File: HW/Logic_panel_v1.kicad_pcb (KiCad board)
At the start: 4 copper layers, 100.1 x 100 mm, 251 parts, among them J1 USB_B_Micro, Q1 Q_NPN_BEC, Q2 Q_NPN_BEC, Q4 Q_NMOS_GSD, Q5 Q_PMOS_GSD, Q6 Q_NMOS_GSD, Q7 Q_PMOS_GSD, Q8 Q_NMOS_GSD, Q9 Q_PMOS_GSD, SW1 SW_SPDT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

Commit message: nicer routing
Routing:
- net Board_1-DATA_hodnoceni_LED: track 88.8 -> 83.7 mm
- net Board_1-BTN_ENTER: track 119.6 -> 115.3 mm
- net Board_1-BARVA_3: track 61.2 -> 56.9 mm
- net Board_1-BARVA_1: track 55.8 -> 51.6 mm
- net Board_1-BARVA_2: track 53.6 -> 49.4 mm
- net Board_1-BTN_NEW_GAME: track 97.0 -> 93.2 mm
- net Board_1-BARVA_5: track 92.9 -> 89.3 mm
- net Board_1-BARVA_4: track 88.8 -> 85.4 mm
- net Board_1-ZAPINANI_2_CAST_LED: track 46.6 -> 44.6 mm
- net Board_1-BARVA_6: track 82.6 -> 80.9 mm
- net Board_1-BTN_SIPKA_VPRAVO: track 42.7 -> 41.4 mm
- net Board_1-EN: track 21.5 -> 20.7 mm

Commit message: repair mistakes
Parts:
- C22: value 4u7 -> 10u
- R15, R17, R19: value 10k -> 100k
- R6: value 2k -> 10k
- R8, R9: value 47k -> 10k
- moved C5 10.8 mm to (64.4, 111.1), turned to 180 degrees
- moved C6 9.47 mm to (53.9, 108.1), turned to 90 degrees
- moved D1 7.06 mm to (67.7, 61.0), turned to 90 degrees
- moved R2 6.98 mm to (67.7, 63.6), turned to 90 degrees
- moved C3 5.16 mm to (64.3, 107.0)
- moved C2 4.53 mm to (63.8, 105.3), turned to 90 degrees
- moved SW1 3.85 mm to (64.2, 52.7)
- moved J1 3.41 mm to (54.3, 67.8)
- moved D7 2.01 mm to (62.1, 65.6)
- moved D8 2.00 mm to (62.1, 63.6)
- moved R18 1.24 mm to (69.9, 108.9)
- moved R17 0.68 mm to (70.1, 91.5)
- moved R19 0.67 mm to (70.0, 113.4)
- moved R8 0.56 mm to (55.0, 92.3)
- moved C4 0.53 mm to (59.8, 102.8)
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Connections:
- J1 pad 6: Board_1-GND -> Board_1-Net-(J1-Pad6)
- R8 pad 2: Board_1-TX_ESP -> Board_1-Net-(R8-Pad2)
- R9 pad 2: Board_1-RX_ESP -> Board_1-Net-(R9-Pad2)
- U2 pad 18: Board_1-Net-(U2-Pad18) -> Board_1-Net-(R9-Pad2)
- U2 pad 19: Board_1-Net-(U2-Pad19) -> Board_1-Net-(R8-Pad2)
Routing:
- net Board_1-+5V: track 86.9 -> 29.2 mm, vias 4 -> 5
- net Board_1-Net-(R9-Pad2): track 0.00 -> 18.4 mm, vias 0 -> 2
- net Board_1-Net-(J1-Pad6): track 0.00 -> 15.5 mm
- net Board_1-Net-(R8-Pad2): track 0.00 -> 13.2 mm, vias 0 -> 2
- net Board_1-DATA_hodnoceni_LED: track 83.7 -> 91.7 mm, vias 2 -> 0
- net Board_1-V_IN: track 13.8 -> 21.3 mm, vias 1 -> 0
- net Board_1-Net-(D8-Pad2): track 23.8 -> 30.2 mm, vias 2 -> 4
- net Board_1-RX_ESP: track 32.1 -> 35.7 mm
- net Board_1-TX_ESP: track 35.1 -> 38.5 mm
- net Board_1-BTN_END: track 23.9 -> 26.1 mm
- net Board_1-BARVA_1: track 51.6 -> 53.6 mm
- net Board_1-BTN_NEW_GAME: track 93.2 -> 94.7 mm
- net Board_1-BTN_ENTER: track 115.3 -> 116.8 mm
- net Board_1-+3V3: track 55.1 -> 56.4 mm, vias 12 -> 11
- net Board_1-GND: track 519.2 -> 518.0 mm, vias 119 -> 123
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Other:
- board text added: "Fialová"
- board text added: "Konec"
- board text added: "Modrá"
- board text added: "Nová hra"
- board text added: "Oranžová"
- board text added: "Potvrdit tah"
- board text added: "Zelená"
- board text added: "Červená"
- board text added: "Šipka vlevo"
- board text added: "Šipka vpravo"
- board text added: "Žlutá"

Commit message: v1.0 for fab
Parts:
- removed the REF** at (58.0, 148.0)
- removed the REF** at (142.1, 52.0)
- added REF**: NPTH, NPTH, F.Cu at (58.0, 148.0)
- added REF**: NPTH, NPTH, F.Cu at (142.0, 52.0)
- moved D8 2.11 mm to (62.0, 65.7)
- moved D7 1.95 mm to (62.0, 63.6)
- moved R16 1.35 mm to (70.1, 87.9)
- moved C22 0.36 mm to (61.7, 81.4)
- moved C23 0.28 mm to (60.6, 81.4)
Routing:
- net Board_1-+3V3: track 56.4 -> 69.1 mm
- net Board_1-Net-(D8-Pad2): track 30.2 -> 24.7 mm, vias 4 -> 2
- net Board_1-Net-(D7-Pad2): track 23.9 -> 28.6 mm
- net Board_1-GND: track 518.0 -> 514.4 mm, vias 123 -> 122
- net Board_1-V_IN: track 21.3 -> 19.5 mm
- net Board_1-/herni_LED.sch/8.sch/DATA_IN: track 40.2 -> 38.8 mm
- net Board_1-V_LED_3: track 206.6 -> 207.4 mm
- net Board_1-V_LED_1: track 302.1 -> 301.3 mm
- net Board_1-ZAPINANI_2_CAST_LED: track 43.8 -> 43.2 mm
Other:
- board size 100.1 x 100 mm -> 100 x 100 mm
- board text added: "Power 3V3"
- board text added: "Power 5V"

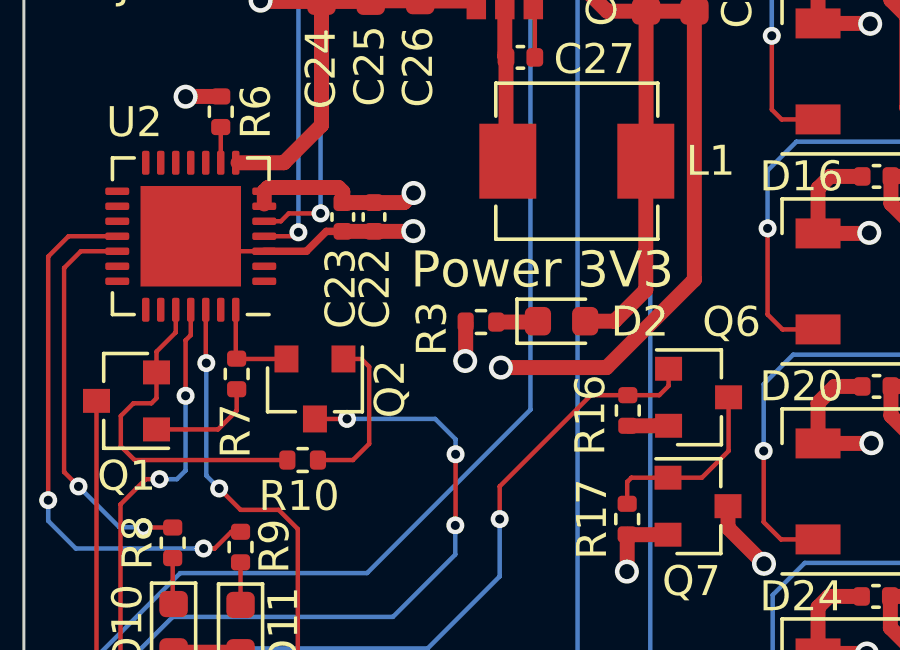
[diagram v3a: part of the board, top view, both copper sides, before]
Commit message: repair mistake in v1.0 - for fab, add to back-up v1.0 folder fab
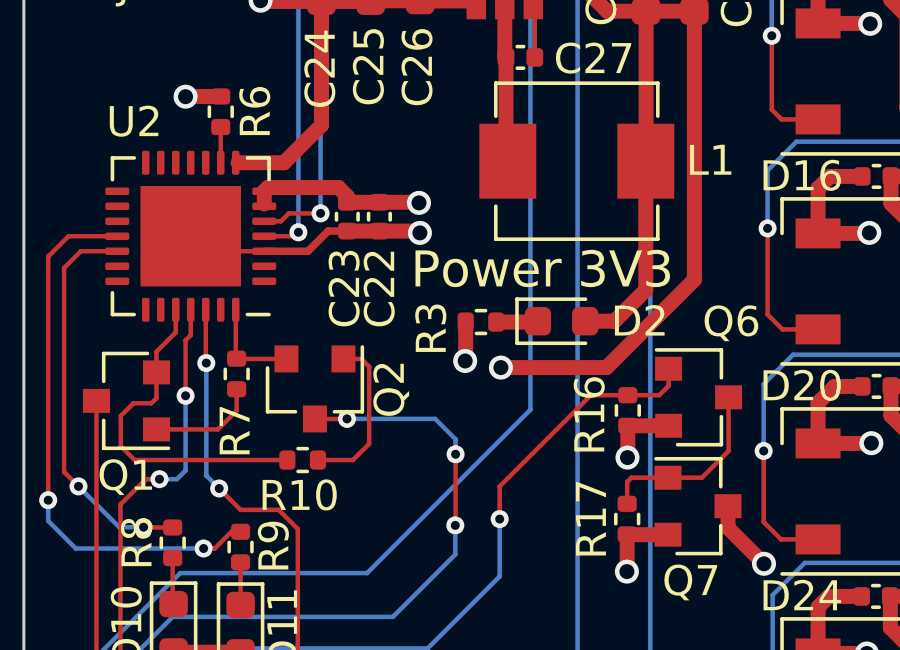
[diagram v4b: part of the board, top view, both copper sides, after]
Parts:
- removed the D5 at (94.5, 56.0)
- removed the U1 at (59.1, 107.5)
- added C20: 10n, Capacitor_SMD:C_0402_1005Metric, F.Cu at (134.1, 139.0)
- added D41: WS2812B, LED_SMD:LED_WS2812B_PLCC4_5.0x5.0mm_P3.2mm, F.Cu at (86.4, 118.5)
- D5: renamed from C20; value 10n -> WS2812B; footprint Capacitor_SMD:C_0402_1005Metric -> LED_SMD:LED_WS2812B_PLCC4_5.0x5.0mm_P3.2mm
- U1: renamed from D41; value WS2812B -> ESP32-PICO-D4; footprint LED_SMD:LED_WS2812B_PLCC4_5.0x5.0mm_P3.2mm -> Package_DFN_QFN:QFN-48-1EP_7x7mm_P0.5mm_EP5.3x5.3mm
- moved D5 91.9 mm to (94.5, 56.0)
- moved U1 29.5 mm to (59.1, 107.5), turned to 270 degrees
- moved C22 0.18 mm to (61.9, 81.4)
- moved C23 0.15 mm to (60.8, 81.4)
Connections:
- D5 pad 1: Board_1-GND -> Board_1-V_LED_1
- D5 pad 2: Board_1-BTN_ENTER -> Board_1-Net-(D5-Pad2)
- U1 pad 1: Board_1-V_LED_3 -> Board_1-+3V3
- U1 pad 2: Board_1-Net-(D41-Pad2) -> Board_1-Net-(U1-Pad2)
- U1 pad 3: Board_1-GND -> Board_1-+3V3
- U1 pad 4: Board_1-Net-(D40-Pad2) -> Board_1-+3V3
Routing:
- net Board_1-GND: track 514.4 -> 515.7 mm, vias 122 -> 123
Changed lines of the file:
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@@
     (thickness 1.6)
     (drawings 92)
-    (tracks 2336)
+    (tracks 2339)
     (zones 0)
     (modules 251)
@@
   )
   (module Capacitor_SMD:C_0402_1005Metric (layer F.Cu)
-    (at 60.630001 81.400001 90)
+    (at 60.780001 81.390001 90)
     (descr "Capacitor SMD 0402 (1005 Metric), square (rectangular) end terminal, IPC_7351 nominal, (Body size source: IPC-SM-782 page 76, https://www.pcb-3d.com/wordpress/wp-content/uploads/ipc-sm-782a_amendment_1_and_2.pdf), generated with kicad-footprint-generator")
     (tags capacitor)
@@
   )
   (module Capacitor_SMD:C_0402_1005Metric (layer F.Cu)
-    (at 61.670001 81.400001 90)
+    (at 61.850001 81.390001 90)
     (descr "Capacitor SMD 0402 (1005 Metric), square (rectangular) end terminal, IPC_7351 nominal, (Body size source: IPC-SM-782 page 76, https://www.pcb-3d.com/wordpress/wp-content/uploads/ipc-sm-782a_amendment_1_and_2.pdf), generated with kicad-footprint-generator")
     (tags capacitor)
@@
   (segment (start 53.871 107.641) (end 53.840001 107.610001) (width 0.25) (layer F.Cu) (net 1))
   (segment (start 55.034978 107.641) (end 53.871 107.641) (width 0.25) (layer F.Cu) (net 1))
-  (segment (start 61.670001 80.920001) (end 60.630001 80.920001) (width 0.5) (layer F.Cu) (net 1))
-  (segment (start 60.630001 80.920001) (end 60.630001 80.560001) (width 0.5) (layer F.Cu) (net 1))
   (segment (start 60.487001 80.417001) (end 58.137001 80.417001) (width 0.5) (layer F.Cu) (net 1))
-  (segment (start 60.630001 80.560001) (end 60.487001 80.417001) (width 0.5) (layer F.Cu) (net 1))
-  (via (at 62.990001 80.600001) (size 0.8) (drill 0.5) (layers F.Cu B.Cu) (net 1))
-  (segment (start 62.670001 80.920001) (end 62.990001 80.600001) (width 0.5) (layer F.Cu) (net 1))
-  (segment (start 61.670001 80.920001) (end 62.670001 80.920001) (width 0.5) (layer F.Cu) (net 1))
+  (segment (start 60.780001 80.910001) (end 61.850001 80.910001) (width 0.5) (layer F.Cu) (net 1))
+  (via (at 63.170001 80.930001) (size 0.8) (drill 0.5) (layers F.Cu B.Cu) (net 1))
+  (segment (start 63.150001 80.910001) (end 63.170001 80.930001) (width 0.5) (layer F.Cu) (net 1))
+  (segment (start 61.850001 80.910001) (end 63.150001 80.910001) (width 0.5) (layer F.Cu) (net 1))
+  (segment (start 60.780001 80.710001) (end 60.487001 80.417001) (width 0.5) (layer F.Cu) (net 1))
+  (segment (start 60.780001 80.910001) (end 60.780001 80.710001) (width 0.5) (layer F.Cu) (net 1))
   (segment (start 63.215001 74.200001) (end 63.210001 74.195001) (width 0.5) (layer F.Cu) (net 2))
   (segment (start 65.080001 74.200001) (end 63.215001 74.200001) (width 0.5) (layer F.Cu) (net 2))
@@
   (segment (start 63.050001 61.556001) (end 63.072001 61.534001) (width 0.5) (layer F.Cu) (net 38))
   (segment (start 63.050001 63.620001) (end 63.050001 61.556001) (width 0.5) (layer F.Cu) (net 38))
-  (segment (start 58.012001 82.542001) (end 59.418001 82.542001) (width 0.25) (layer F.Cu) (net 38))
-  (segment (start 60.080001 81.880001) (end 60.630001 81.880001) (width 0.25) (layer F.Cu) (net 38))
-  (segment (start 59.418001 82.542001) (end 60.080001 81.880001) (width 0.25) (layer F.Cu) (net 38))
-  (segment (start 60.630001 81.880001) (end 61.670001 81.880001) (width 0.5) (layer F.Cu) (net 38))
-  (via (at 62.980001 81.870001) (size 0.8) (drill 0.5) (layers F.Cu B.Cu) (net 38))
-  (segment (start 62.970001 81.880001) (end 62.980001 81.870001) (width 0.5) (layer F.Cu) (net 38))
-  (segment (start 61.670001 81.880001) (end 62.970001 81.880001) (width 0.5) (layer F.Cu) (net 38))
   (segment (start 71.490001 88.360001) (end 70.130001 88.360001) (width 0.5) (layer F.Cu) (net 38))
+  (segment (start 60.780001 81.870001) (end 61.850001 81.870001) (width 0.5) (layer F.Cu) (net 38))
+  (via (at 63.200001 81.930001) (size 0.8) (drill 0.5) (layers F.Cu B.Cu) (net 38))
+  (segment (start 63.140001 81.870001) (end 63.200001 81.930001) (width 0.5) (layer F.Cu) (net 38))
+  (segment (start 61.850001 81.870001) (end 63.140001 81.870001) (width 0.5) (layer F.Cu) (net 38))
+  (segment (start 60.140001 81.870001) (end 60.780001 81.870001) (width 0.25) (layer F.Cu) (net 38))
+  (segment (start 59.468001 82.542001) (end 60.140001 81.870001) (width 0.25) (layer F.Cu) (net 38))
+  (segment (start 58.012001 82.542001) (end 59.468001 82.542001) (width 0.25) (layer F.Cu) (net 38))
+  (via (at 70.120001 89.420001) (size 0.8) (drill 0.5) (layers F.Cu B.Cu) (net 38))
+  (segment (start 70.130001 89.410001) (end 70.120001 89.420001) (width 0.5) (layer F.Cu) (net 38))
+  (segment (start 70.130001 88.360001) (end 70.130001 89.410001) (width 0.5) (layer F.Cu) (net 38))
   (via (at 60.770001 88.130001) (size 0.6) (drill 0.3) (layers F.Cu B.Cu) (net 39))
   (segment (start 60.768001 88.132001) (end 60.770001 88.130001) (width 0.15) (layer F.Cu) (net 39))
@@
   (segment (start 62.430001 67.410001) (end 62.420001 67.420001) (width 0.15) (layer F.Cu) (net 95))
   (segment (start 62.430001 64.140001) (end 62.430001 67.410001) (width 0.15) (layer F.Cu) (net 95))
-  (segment (start 58.012001 81.542001) (end 58.568001 81.542001) (width 0.15) (layer F.Cu) (net 95))
   (via (at 59.890001 81.280001) (size 0.6) (drill 0.3) (layers F.Cu B.Cu) (net 95))
-  (segment (start 58.830001 81.280001) (end 59.890001 81.280001) (width 0.15) (layer F.Cu) (net 95))
-  (segment (start 58.568001 81.542001) (end 58.830001 81.280001) (width 0.15) (layer F.Cu) (net 95))
-  (segment (start 59.890001 81.280001) (end 59.890001 71.780001) (width 0.15) (layer B.Cu) (net 95))
+  (segment (start 58.012001 81.542001) (end 58.568001 81.542001) (width 0.15) (layer F.Cu) (net 95))
   (segment (start 62.420001 69.250001) (end 62.420001 67.420001) (width 0.15) (layer B.Cu) (net 95))
+  (segment (start 58.568001 81.542001) (end 58.830001 81.280001) (width 0.15) (layer F.Cu) (net 95))
+  (segment (start 58.830001 81.280001) (end 59.890001 81.280001) (width 0.15) (layer F.Cu) (net 95))
   (segment (start 59.890001 71.780001) (end 62.420001 69.250001) (width 0.15) (layer B.Cu) (net 95))
+  (segment (start 59.890001 81.280001) (end 59.890001 71.780001) (width 0.15) (layer B.Cu) (net 95))
   (segment (start 142.376001 98.982001) (end 142.376001 97.856001) (width 0.15) (layer F.Cu) (net 96))
   (segment (start 142.376001 97.856001) (end 141.790001 97.270001) (width 0.15) (layer F.Cu) (net 96))
@@
   (via (at 61.620283 67.398676) (size 0.6) (drill 0.3) (layers F.Cu B.Cu) (net 103))
   (segment (start 61.490001 65.680001) (end 61.620283 65.810283) (width 0.15) (layer F.Cu) (net 103))
-  (via (at 59.150003 81.910001) (size 0.6) (drill 0.3) (layers F.Cu B.Cu) (net 103))
-  (segment (start 59.018003 82.042001) (end 59.150003 81.910001) (width 0.15) (layer F.Cu) (net 103))
-  (segment (start 58.012001 82.042001) (end 59.018003 82.042001) (width 0.15) (layer F.Cu) (net 103))
-  (segment (start 59.150003 81.910001) (end 59.150003 71.559999) (width 0.15) (layer B.Cu) (net 103))
   (segment (start 59.150003 71.559999) (end 61.620283 69.089719) (width 0.15) (layer B.Cu) (net 103))
+  (segment (start 59.150003 81.910001) (end 59.150003 71.559999) (width 0.15) (layer B.Cu) (net 103))
   (segment (start 61.620283 69.089719) (end 61.620283 67.398676) (width 0.15) (layer B.Cu) (net 103))
+  (segment (start 59.018003 82.042001) (end 59.150003 81.910001) (width 0.15) (layer F.Cu) (net 103))
+  (via (at 59.150003 81.910001) (size 0.6) (drill 0.3) (layers F.Cu B.Cu) (net 103))
+  (segment (start 58.012001 82.042001) (end 59.018003 82.042001) (width 0.15) (layer F.Cu) (net 103))
   (segment (start 126.626001 119.982001) (end 126.626001 118.866001) (width 0.15) (layer F.Cu) (net 104))
   (segment (start 126.626001 118.866001) (end 126.000001 118.240001) (width 0.15) (layer F.Cu) (net 104))

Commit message: v1.0 for fab (for great success once again)
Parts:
- removed the D2 at (67.9, 84.9)
- removed the SW7 at (52.4, 124.2)
- removed the U1 at (59.1, 107.5)
- added C76: 100n, Capacitor_SMD:C_0402_1005Metric, F.Cu at (128.8, 72.9)
- added D84: WS2812B, LED_SMD:LED_WS2812B_PLCC4_5.0x5.0mm_P3.2mm, F.Cu at (121.1, 125.4)
- added R12: 36k, Resistor_SMD:R_0603_1608Metric, F.Cu at (64.9, 68.7)
- D2: renamed from C76; value 100n -> green; footprint Capacitor_SMD:C_0402_1005Metric -> LED_SMD:LED_0603_1608Metric
- SW7: renamed from R12; value 36k -> button; footprint Resistor_SMD:R_0603_1608Metric -> Button_Switch_THT:SW_PUSH_6mm
- U1: renamed from D84; value WS2812B -> ESP32-PICO-D4; footprint LED_SMD:LED_WS2812B_PLCC4_5.0x5.0mm_P3.2mm -> Package_DFN_QFN:QFN-48-1EP_7x7mm_P0.5mm_EP5.3x5.3mm
- moved U1 64.5 mm to (59.1, 107.5), turned to 270 degrees
- moved D2 62.1 mm to (67.9, 84.9), turned to 0 degrees
- moved SW7 56.9 mm to (52.4, 124.2), turned to 90 degrees
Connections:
- D2 pad 1: Board_1-V_LED_1 -> Board_1-Net-(D2-Pad1)
- D2 pad 2: Board_1-GND -> Board_1-+3V3
- SW7 pad 1: Board_1-Net-(C28-Pad1) -> Board_1-BTN_END
- U1 pad 1: Board_1-V_LED_3 -> Board_1-+3V3
- U1 pad 2: Board_1-Net-(D84-Pad2) -> Board_1-Net-(U1-Pad2)
- U1 pad 3: Board_1-GND -> Board_1-+3V3
- U1 pad 4: Board_1-/hodnoceni_LED.sch/9.sch/DATA_IN -> Board_1-+3V3
